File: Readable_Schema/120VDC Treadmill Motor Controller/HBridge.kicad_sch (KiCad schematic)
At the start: 0 parts

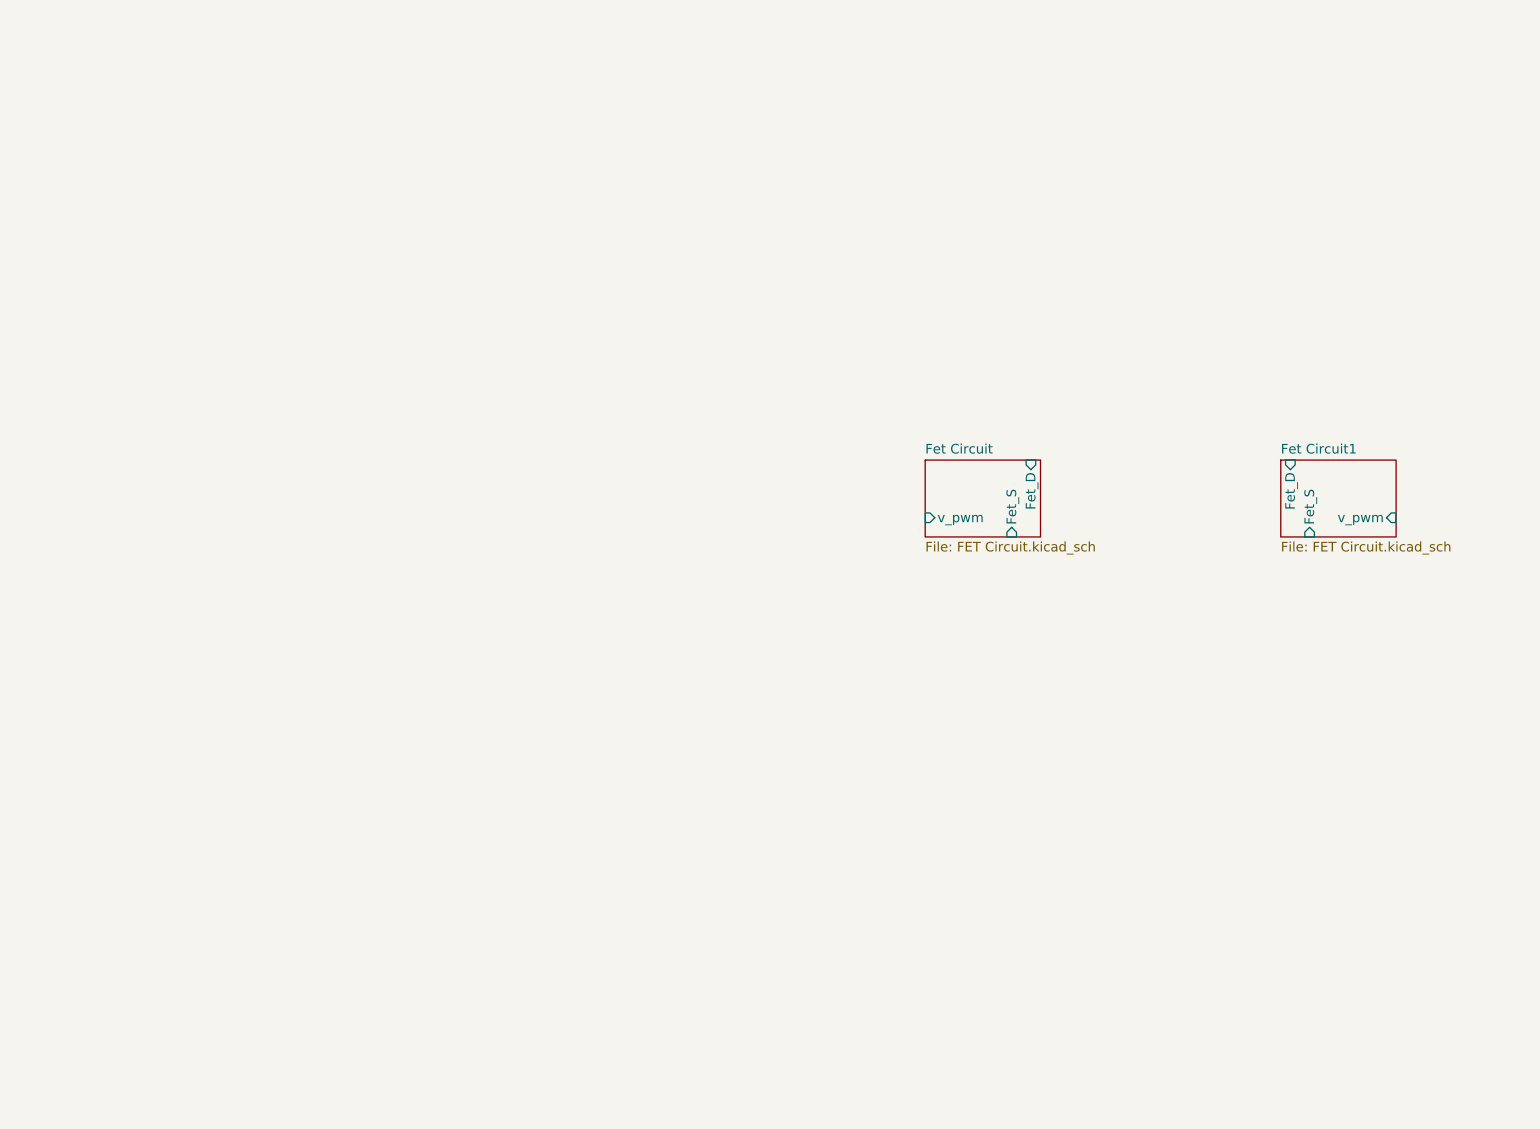
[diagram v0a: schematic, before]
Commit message: I cant for the life of me get the current sensing to actually properly scale with current, I treid 5 different sim models and right now the DA is the best but doesnt start showing anything till around 19amps which kind of defeats the purpose
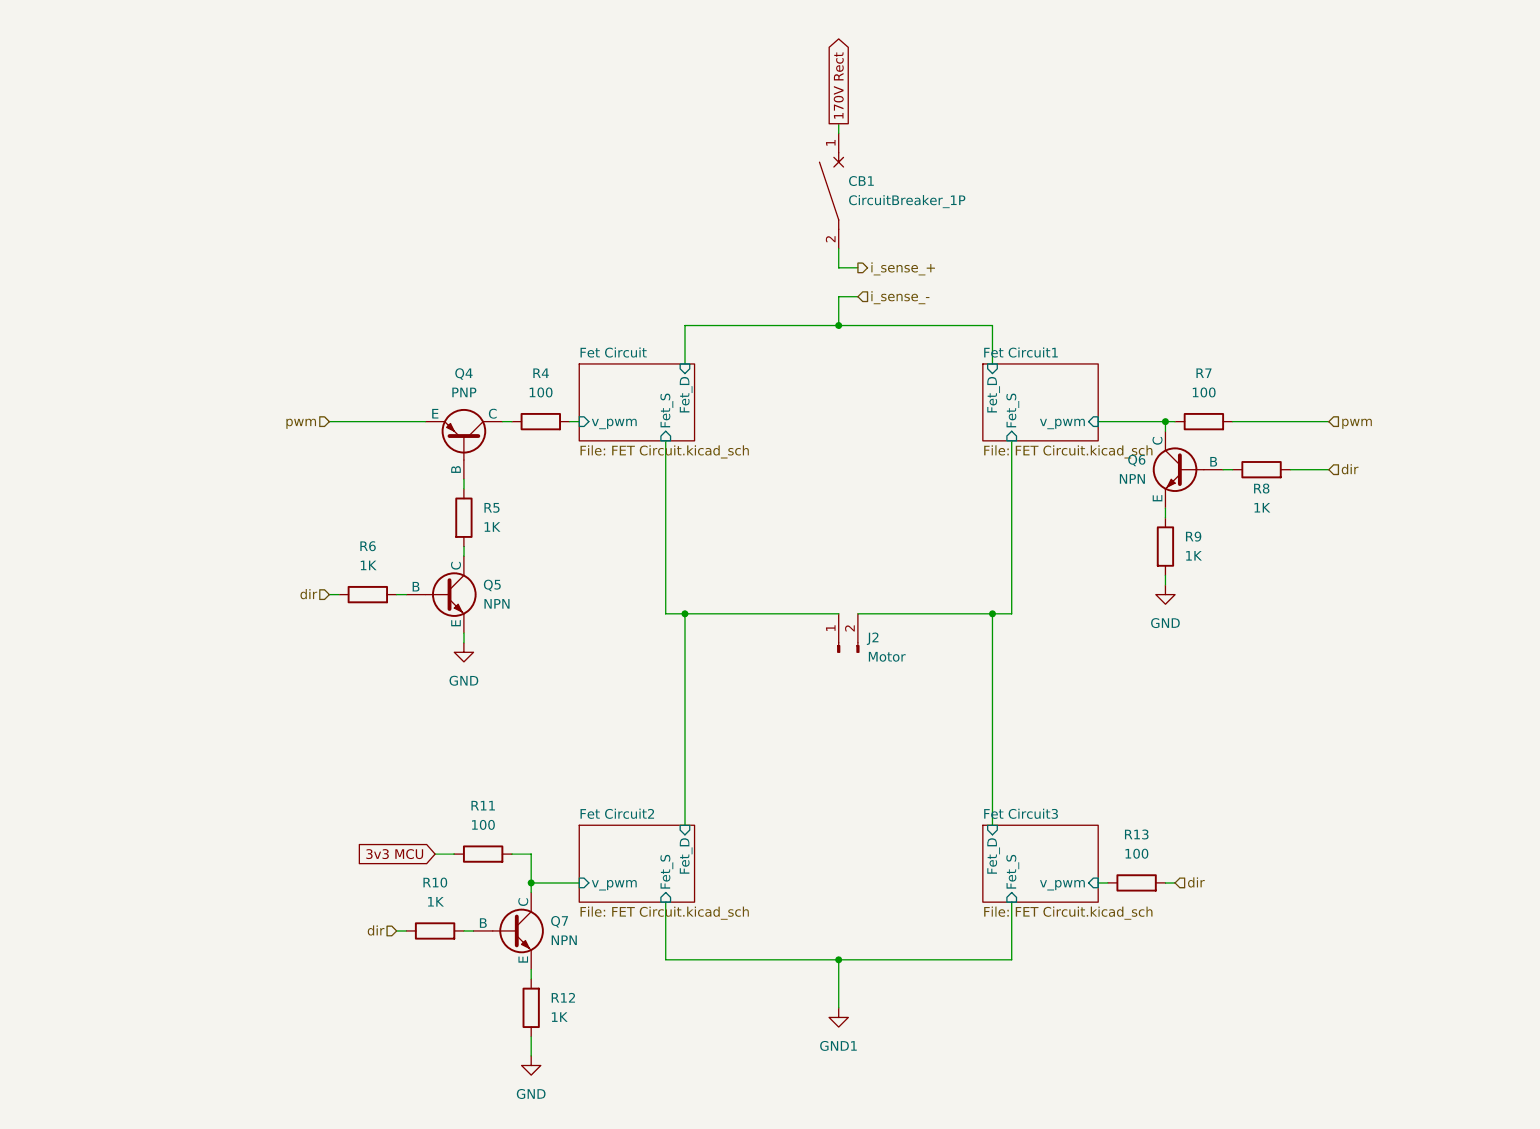
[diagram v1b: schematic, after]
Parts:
- added CB1: CircuitBreaker_1P, symbol Device:CircuitBreaker_1P
- added J2: Motor, symbol Connector:Conn_01x02_Pin
- added Q4: PNP, symbol Simulation_SPICE:PNP
- added Q5, Q6, Q7: NPN, symbol Simulation_SPICE:NPN
- added R10, R12, R5, R6, R8, R9: 1K, symbol Device:R
- added R11, R13, R4, R7: 100, symbol Device:R
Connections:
- net Fet Circuit/Fet_S: now also J2.1 (Pin_1)
- net Fet Circuit/v_pwm: now also R4.2
- net Fet Circuit1/Fet_S: now also J2.2 (Pin_2)
- net Fet Circuit1/v_pwm: now also Q6.1 (C), R7.1
- new net: Q4.2 (B), R5.1
- new net: Q5.1 (C), R5.2
- new net: Q6.2 (B), R8.1
- new net: Q6.3 (E), R9.1
- new net: Q7.3 (E), R12.2
- new net: Q5.2 (B), R6.2
- new net: Q7.2 (B), R10.2
- new net: Q4.1 (C), R4.1
- new net 170V Rect: CB1.1
- new net 3v3 MCU: R11.1
- new net Fet Circuit2/v_pwm: Q7.1 (C), R11.2
- new net Fet Circuit3/v_pwm: R13.1
- new net GND: Q5.3 (E), R12.1, R9.2
- new net dir: R10.1, R13.2, R6.1, R8.2
- new net i_sense_+: CB1.2
- new net pwm: Q4.3 (E), R7.2
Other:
- added sheet Fet Circuit2 (FET Circuit.kicad_sch)
- added sheet Fet Circuit3 (FET Circuit.kicad_sch)

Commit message: Tried better simulating back emf with little success, started adding footprints and real components to the readable schema (kicad)
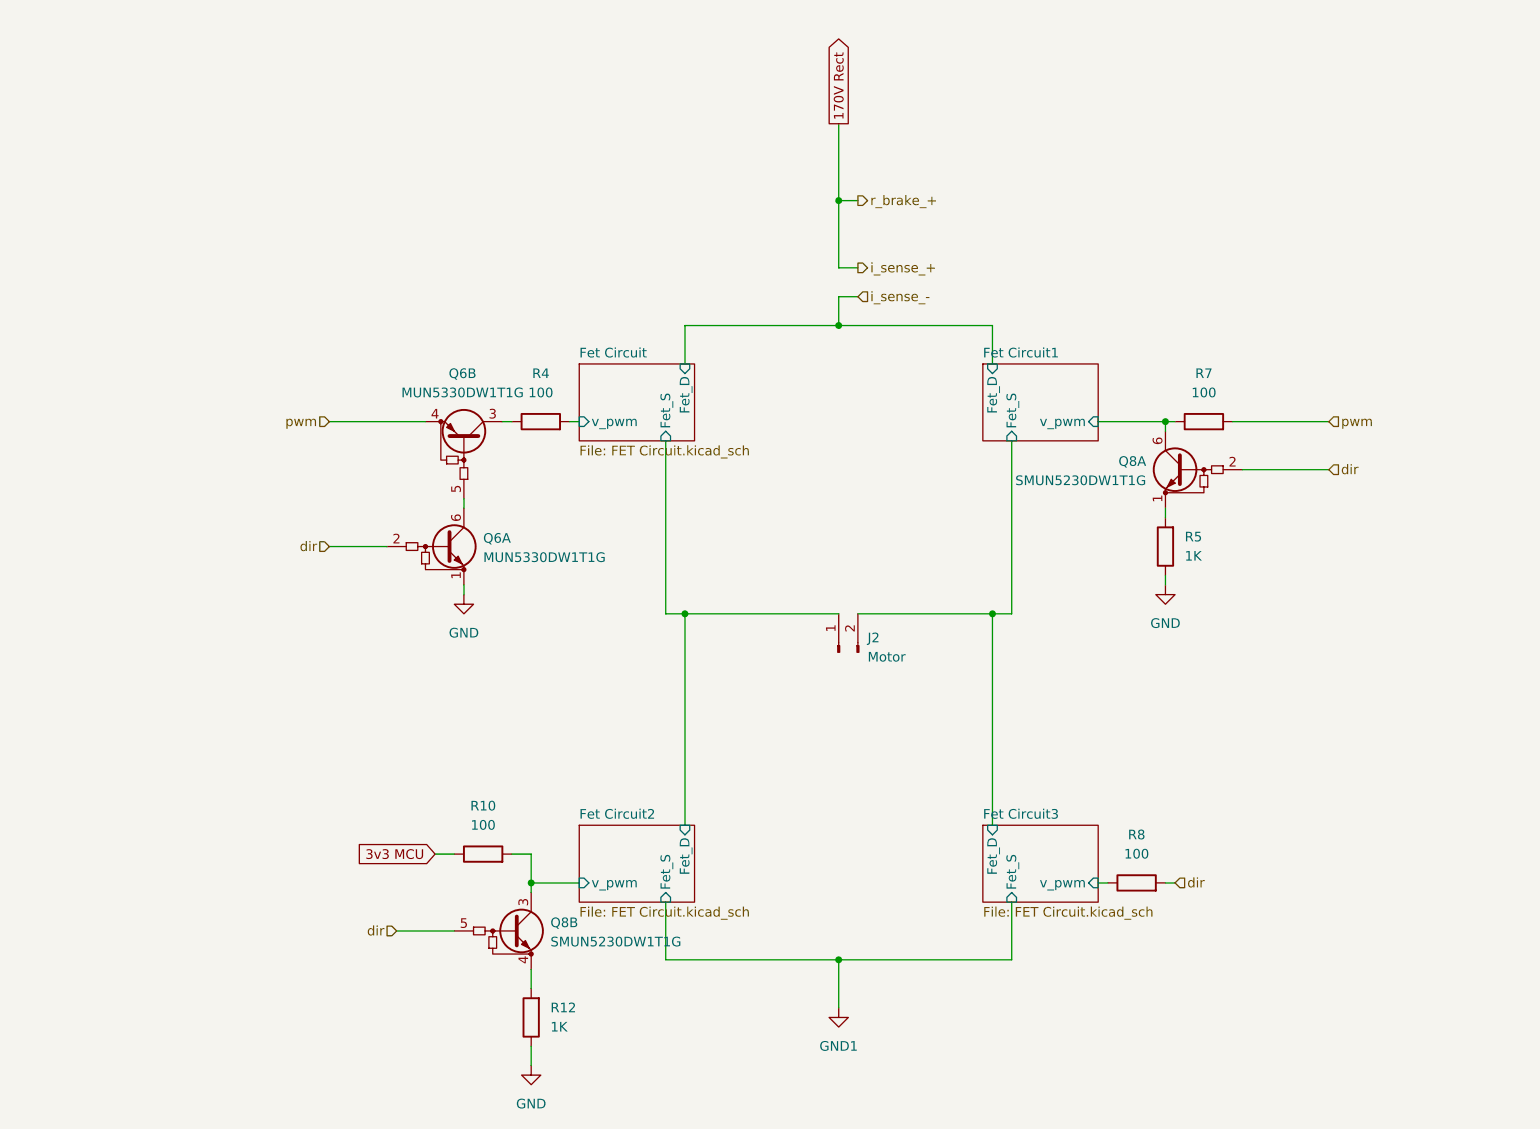
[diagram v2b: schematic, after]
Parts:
- removed CB1: CircuitBreaker_1P, symbol Device:CircuitBreaker_1P
- removed Q4: PNP, symbol Simulation_SPICE:PNP
- removed Q5, Q6, Q7: NPN, symbol Simulation_SPICE:NPN
- removed R11, R13: 100, symbol Device:R
- removed R6, R9: 1K, symbol Device:R
- added Q6: MUN5330DW1T1G, Package_TO_SOT_SMD:SOT-363_SC-70-6, symbol Transistor_BJT:MUN5330DW1
- added Q8: SMUN5230DW1T1G, Package_TO_SOT_SMD:SOT-363_SC-70-6, symbol Transistor_BJT:MUN5211DW1
- R10, R8: value 1K -> 100; footprint (none) -> Resistor_SMD:R_1206_3216Metric_Pad1.30x1.75mm_HandSolder
- R12, R5: footprint (none) -> Resistor_SMD:R_0805_2012Metric_Pad1.20x1.40mm_HandSolder
- R4, R7: footprint (none) -> Resistor_SMD:R_1206_3216Metric_Pad1.30x1.75mm_HandSolder
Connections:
- net 3v3 MCU: now also R10.1
- net Fet Circuit1/v_pwm: now also Q8.6 (C1)
- net Fet Circuit2/v_pwm: now also R10.2, Q8.3 (C2)
- net Fet Circuit3/v_pwm: now also R8.1
- net GND: now also R5.1, Q6.1 (E1)
- net dir: now also Q6.2 (B1), Q8.2 (B1), Q8.5 (B2); no longer R10.1
- net pwm: now also Q6.4 (E2)
- net at R5.2: now also Q8.1 (E1)
- net at R12.2: now also Q8.4 (E2)
- net at R4.1: now also Q6.3 (C2)
- new net: Q6.5 (B2), Q6.6 (C1)
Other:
- moved on the sheet: R12

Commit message: Updated some more footprints and started learning about base resistor sizing and the importance of Pavg rather than Ppeak. changed low side fets in kicad to use a shared power supply
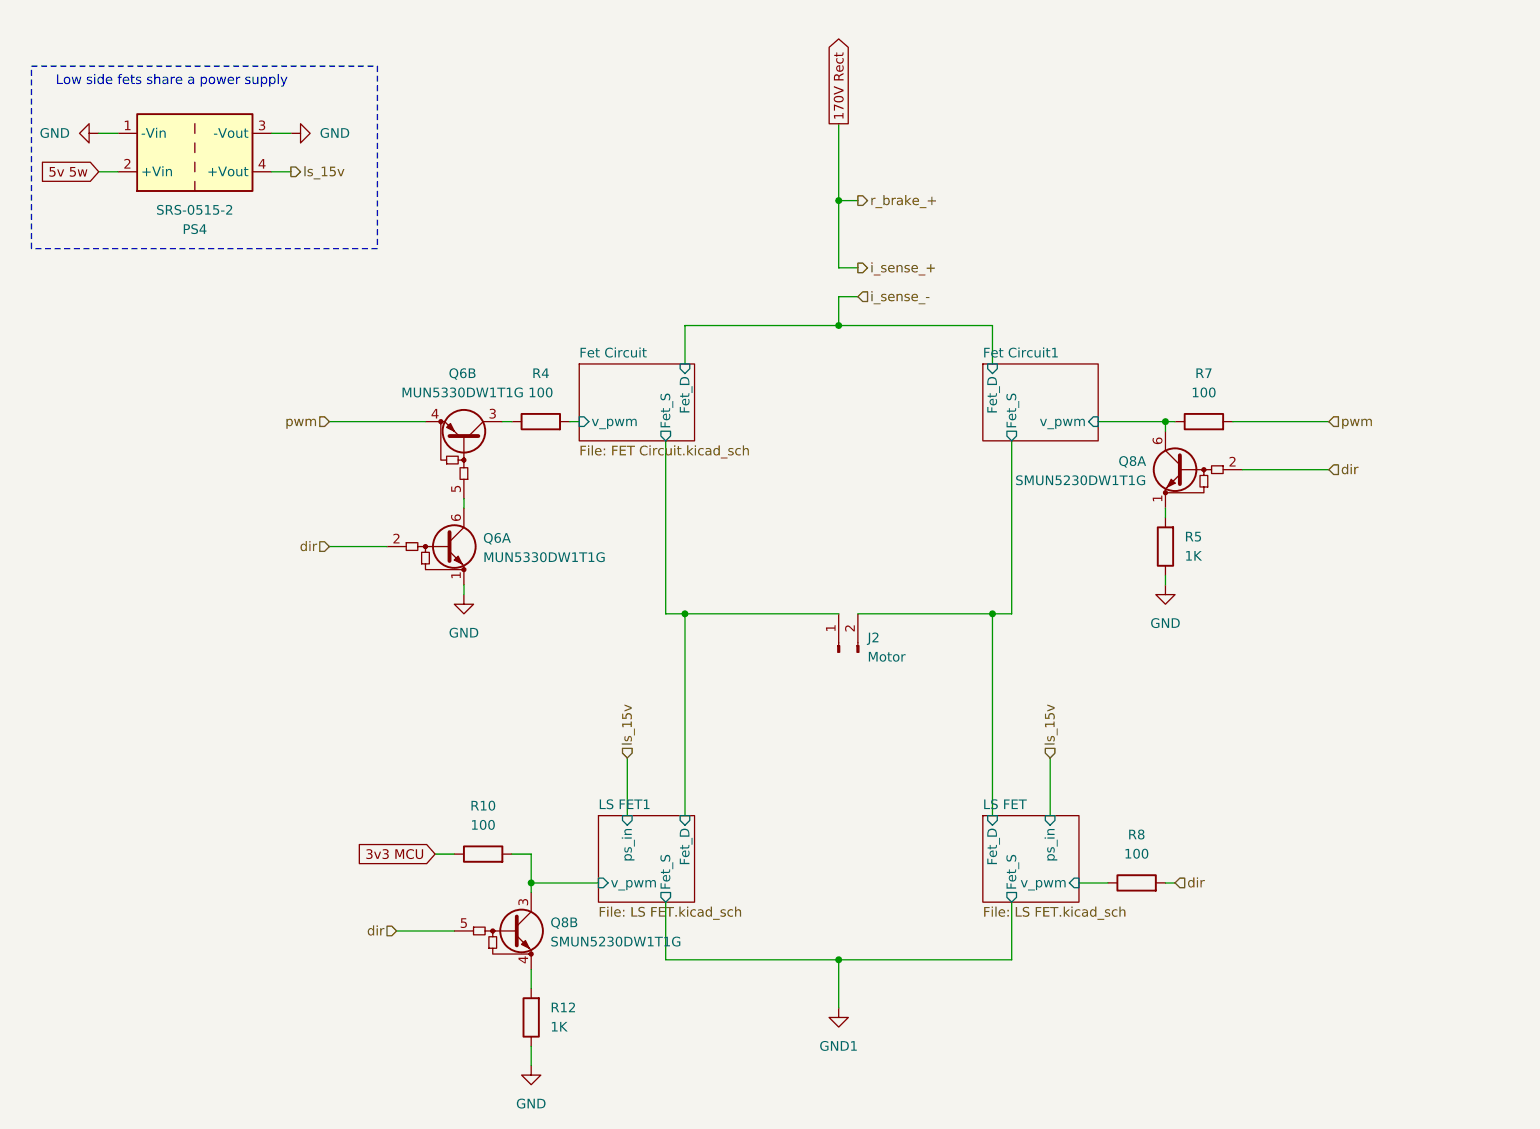
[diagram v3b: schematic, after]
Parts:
- added PS4: SRS-0515-2, Footprints_TMC:SRS-0515 DIP-16_W7.62mm, symbol Converter_DCDC:MEE1S0303SC
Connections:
- net GND: now also PS4.1 (-Vin), PS4.3 (-Vout)
- net Fet Circuit2/v_pwm renamed LS FET1/v_pwm
- net Fet Circuit3/v_pwm renamed LS FET/v_pwm
- new net 5v 5w: PS4.2 (+Vin)
- new net ls_15v: PS4.4 (+Vout)
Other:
- removed sheet Fet Circuit2
- removed sheet Fet Circuit3
- added sheet LS FET (LS FET.kicad_sch)
- added sheet LS FET1 (LS FET.kicad_sch)
- note added: "Low side fets share a power supply"
